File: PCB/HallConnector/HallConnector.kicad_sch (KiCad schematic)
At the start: 13 parts, among them CN3 WAFER-SH1.0-4PWB, J1 Conn_01x05_Pin, U1 WAFER-SH1.0-2PWB, U2 WAFER-SH1.0-2PWB

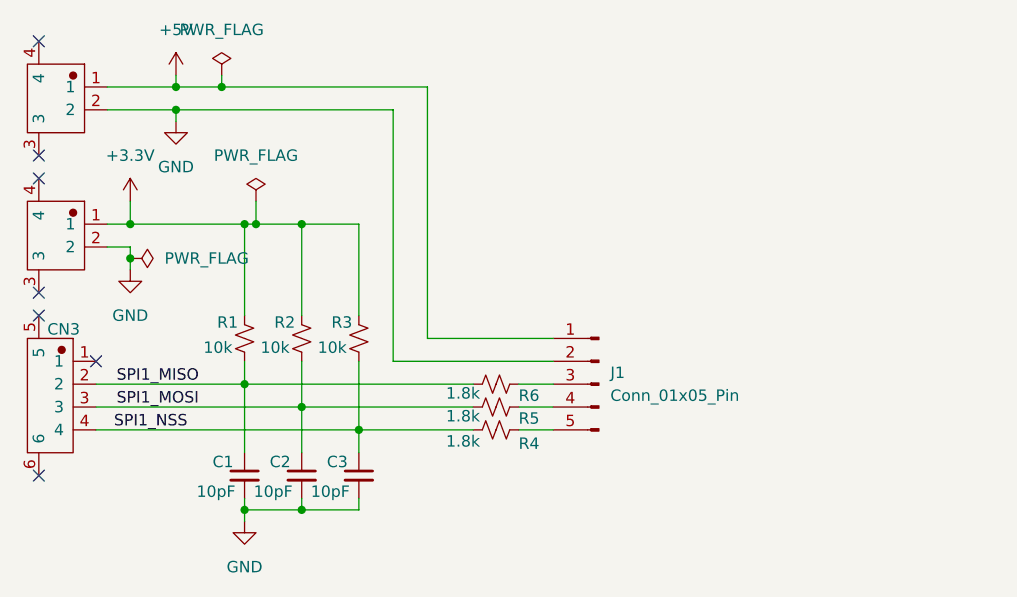
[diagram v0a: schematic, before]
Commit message: 修复霍尔接口板线序问题，完成串口测试
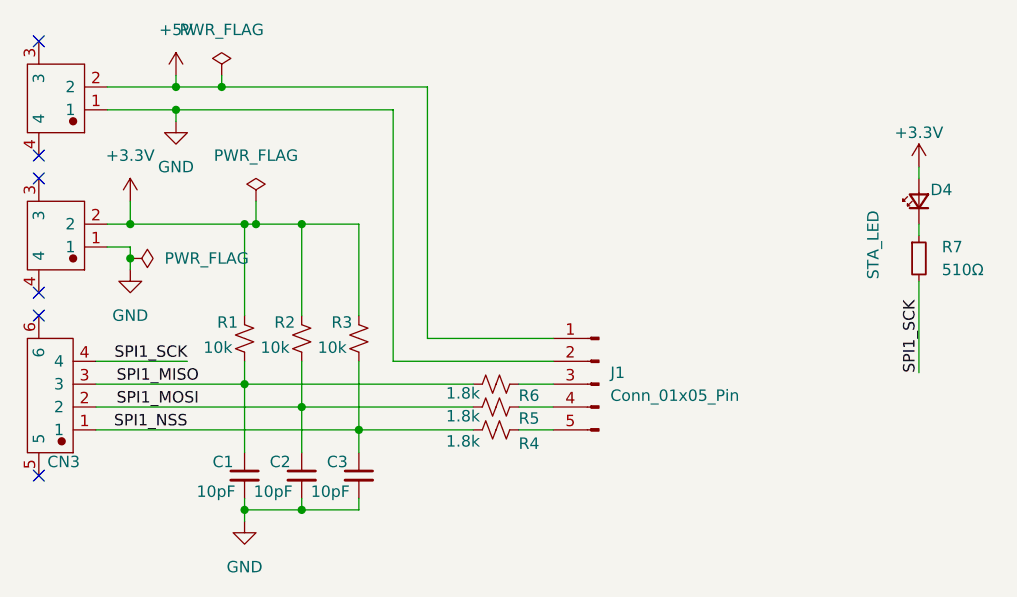
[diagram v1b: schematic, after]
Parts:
- added D4: STA_LED, LED_SMD:LED_0603_1608Metric_Pad1.05x0.95mm_HandSolder, symbol Device:LED_Small
- added R7: 510Ω, Resistor_SMD:R_0603_1608Metric_Pad0.98x0.95mm_HandSolder, symbol Device:R_Small
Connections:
- net +3.3V: now also U1.2, D4.2 (A); no longer U1.1
- net +5V: now also U2.2; no longer U2.1
- net GND: now also U1.1, U2.1; no longer U1.2, U2.2
- net SPI1_MISO: now also CN3.3; no longer CN3.2
- net SPI1_MOSI: now also CN3.2; no longer CN3.3
- net SPI1_NSS: now also CN3.1; no longer CN3.4
- new net: D4.1 (K), R7.1
- new net SPI1_SCK: CN3.4, R7.2
- no-connect marks 7 -> 6
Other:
- moved on the sheet: CN3
